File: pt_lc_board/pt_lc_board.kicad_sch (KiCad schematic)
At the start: 32 parts, among them J1 DSUB1, J2 DSUB2, J3 DSUB3, J4 PCIE Socket, U1 HX711_Breakout, U10 PCF8575_Breakout, U2 HX711_Breakout, U3 HX711_Breakout, U4 HX711_Breakout, U5 HX711_Breakout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

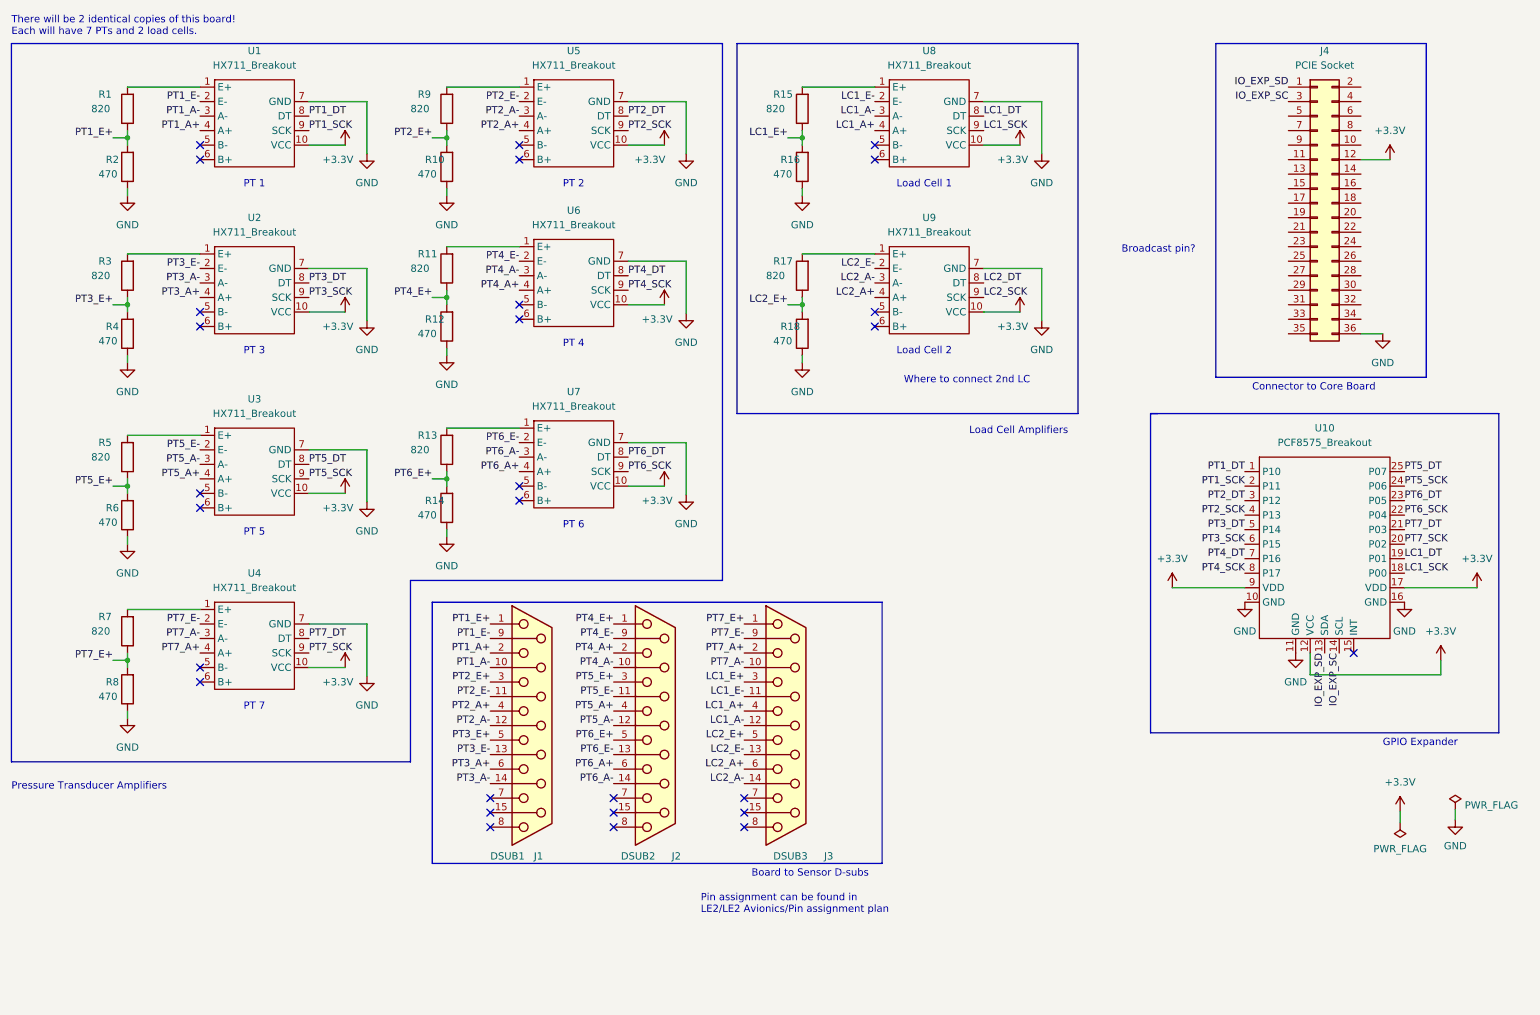
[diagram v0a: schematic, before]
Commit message: Almost done with layout. Need board-to-board connection.
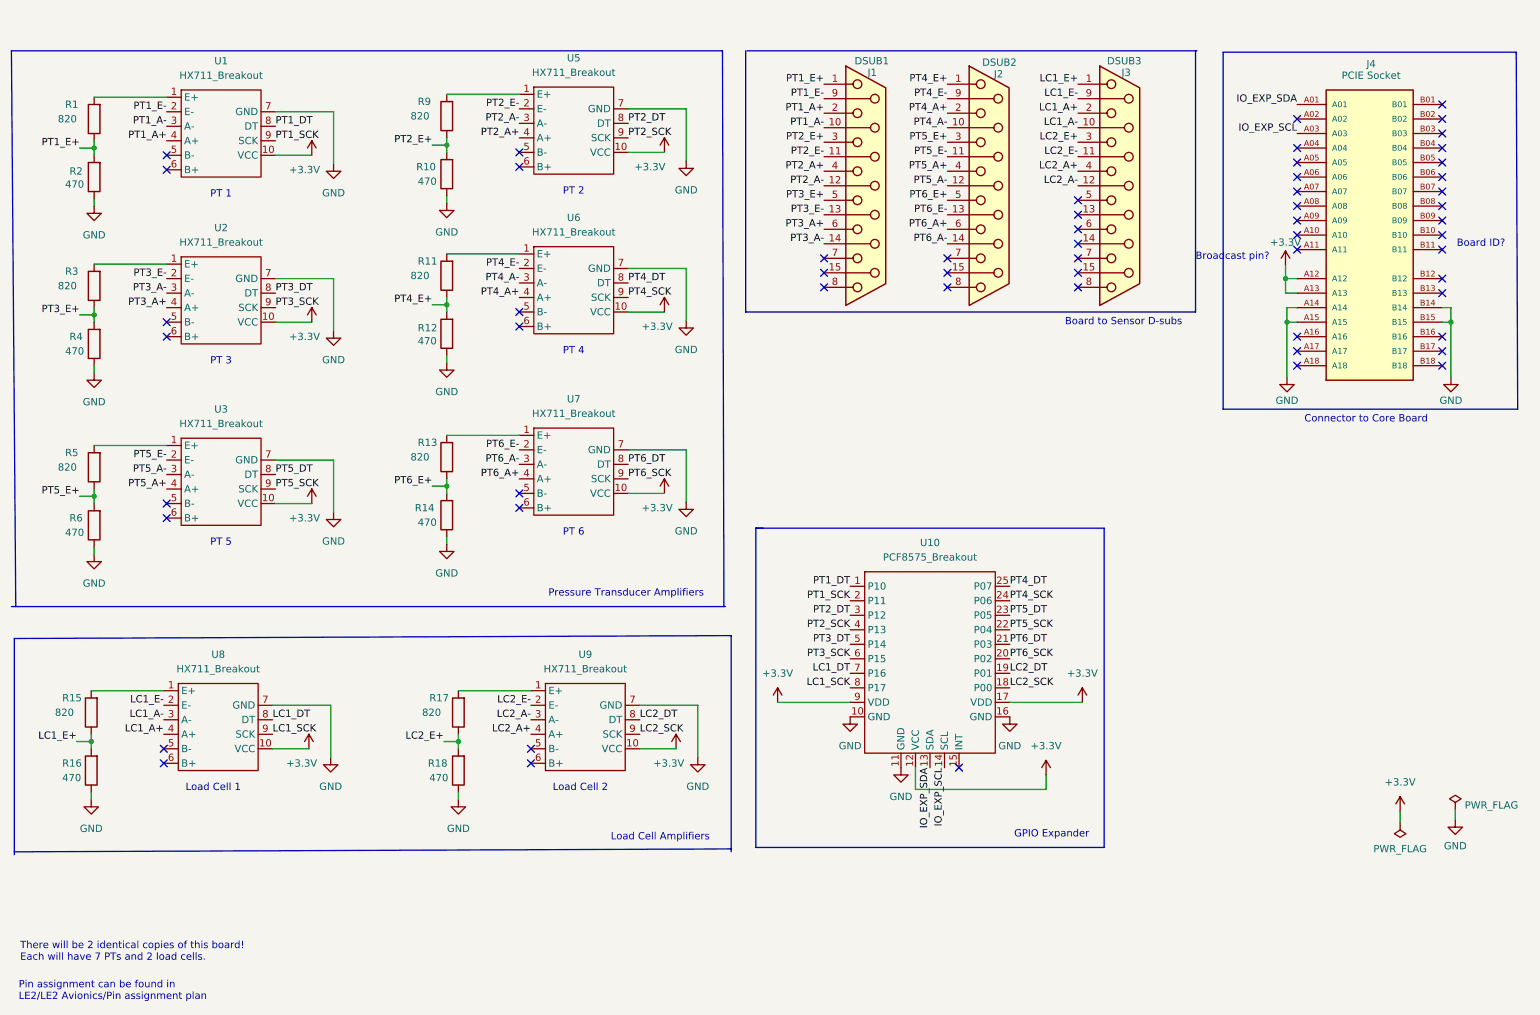
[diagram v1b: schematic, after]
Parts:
- removed R7: 820, Resistor_SMD:R_1206_3216Metric, symbol Device:R
- removed R8: 470, Resistor_SMD:R_1206_3216Metric, symbol Device:R
- removed U4: HX711_Breakout, symbol ELLIE_Symbol_Library:HX711_Breakout
- J1, J2, J3: footprint (none) -> Connector_Dsub:DSUB-15_Female_Horizontal_P2.77x2.84mm_EdgePinOffset7.70mm_Housed_MountingHolesOffset9.12mm
- J4: footprint (none) -> PCIE-LP-01-01-F-DV-A-TR:SAMTEC_PCIE-LP-01-01-F-DV-A-TR; symbol Connector_Generic:Conn_02x18_Odd_Even -> PCIE:PCIE-LP-01-01-F-DV-A-TR; MANUFACTURER (none) -> Samtec; MAXIMUM_PACKAGE_HEIGHT (none) -> 8.13mm; PARTREV (none) -> B; STANDARD (none) -> Manufacturer Recommendations
- U1, U2, U3, U5, U6, U7, U8, U9: footprint (none) -> Ellie_Project_Footprints:HX711_Breakout_Board
- U10: footprint (none) -> PCF8575_Breakout:PCF8575_Breakout
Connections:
- net PT7_A+ is gone; now on net LC1_A+: J3.2
- net PT7_A- is gone; now on net LC1_A-: J3.10 (P10)
- net PT7_DT is gone; now on net PT6_DT: U10.21 (P03)
- net PT7_E+ is gone; now on net LC1_E+: J3.1
- net PT7_E- is gone; now on net LC1_E-: J3.9 (P9)
- net PT7_SCK is gone; now on net PT6_SCK: U10.20 (P02)
- net +3V3: now also J4.A12, J4.A13; no longer J4.12 (Pin_12)
- net GND: now also J4.A14, J4.A15, J4.B14, J4.B15; no longer J4.36 (Pin_36)
- net LC1_A+: no longer J3.4
- net LC1_A-: no longer J3.12 (P12)
- net LC1_DT: now also U10.7 (P16); no longer U10.19 (P01)
- net LC1_E+: no longer J3.3
- net LC1_E-: no longer J3.11 (P111)
- net LC1_SCK: now also U10.8 (P17); no longer U10.18 (P00)
- net LC2_A+: now also J3.4; no longer J3.6
- net LC2_A-: now also J3.12 (P12); no longer J3.14 (P14)
- net LC2_DT: now also U10.19 (P01)
- net LC2_E+: now also J3.3; no longer J3.5
- net LC2_E-: now also J3.11 (P111); no longer J3.13 (P13)
- net LC2_SCK: now also U10.18 (P00)
- net PT4_DT: now also U10.25 (P07); no longer U10.7 (P16)
- net PT4_SCK: now also U10.24 (P06); no longer U10.8 (P17)
- net PT5_DT: now also U10.23 (P05); no longer U10.25 (P07)
- net PT5_SCK: now also U10.22 (P04); no longer U10.24 (P06)
- net PT6_DT: no longer U10.23 (P05)
- net PT6_SCK: no longer U10.22 (P04)
- net IO_EXP_SC renamed IO_EXP_SCL
- net IO_EXP_SCL: now also J4.A03; no longer J4.3 (Pin_3)
- net IO_EXP_SD renamed IO_EXP_SDA
- net IO_EXP_SDA: now also J4.A01; no longer J4.1 (Pin_1)
- no-connect marks 28 -> 58
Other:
- note added: "Board ID?"
- note removed: "PT 7"
- note removed: "Where to connect 2nd LC"
- moved on the sheet: J1, J2, J3, J4, R1, R10, R11, R12, R13, R14, R15, R16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

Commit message: Mostly finished with board.
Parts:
- added R10, R11, R9: 4.7k, Resistor_SMD:R_0603_1608Metric, symbol Device:R
- J4: value PCIE Socket -> PCIE Card Edge; footprint PCIE-LP-01-01-F-DV-A-TR:SAMTEC_PCIE-LP-01-01-F-DV-A-TR -> Connector_PCBEdge:BUS_PCIexpress_x1; symbol PCIE:PCIE-LP-01-01-F-DV-A-TR -> PCIE:PCIE-LP-01-01-F-DV-A-TR_(card_edge)
- R1, R13, R17: footprint Resistor_SMD:R_1206_3216Metric -> Resistor_SMD:R_0603_1608Metric
- R12: renamed from R5; footprint Resistor_SMD:R_1206_3216Metric -> Resistor_SMD:R_0603_1608Metric
- R14: renamed from R6; footprint Resistor_SMD:R_1206_3216Metric -> Resistor_SMD:R_0603_1608Metric
- R15: renamed from R14; footprint Resistor_SMD:R_1206_3216Metric -> Resistor_SMD:R_0603_1608Metric
- R16: renamed from R15; footprint Resistor_SMD:R_1206_3216Metric -> Resistor_SMD:R_0603_1608Metric
- R18: renamed from R16; footprint Resistor_SMD:R_1206_3216Metric -> Resistor_SMD:R_0603_1608Metric
- R19: renamed from R18; footprint Resistor_SMD:R_1206_3216Metric -> Resistor_SMD:R_0603_1608Metric
- R2: renamed from R9; footprint Resistor_SMD:R_1206_3216Metric -> Resistor_SMD:R_0603_1608Metric
- R3: renamed from R2; footprint Resistor_SMD:R_1206_3216Metric -> Resistor_SMD:R_0603_1608Metric
- R4: renamed from R10; footprint Resistor_SMD:R_1206_3216Metric -> Resistor_SMD:R_0603_1608Metric
- R5: renamed from R3; footprint Resistor_SMD:R_1206_3216Metric -> Resistor_SMD:R_0603_1608Metric
- R6: renamed from R11; footprint Resistor_SMD:R_1206_3216Metric -> Resistor_SMD:R_0603_1608Metric
- R7: renamed from R4; footprint Resistor_SMD:R_1206_3216Metric -> Resistor_SMD:R_0603_1608Metric
- R8: renamed from R12; footprint Resistor_SMD:R_1206_3216Metric -> Resistor_SMD:R_0603_1608Metric
- renumbered U5 to U2, U2 to U3, U6 to U4, U3 to U5, U7 to U6, U10 to U7
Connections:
- net GND: now also R10.1, R11.1
- net IO_EXP_SCL: now also J4.A3; no longer J4.A03
- net IO_EXP_SDA: now also J4.A1; no longer J4.A01
- net Board_ID: now reaches J4.B11
- net Board_ID: now also R10.2, R11.2, R9.1
- net +5V: now reaches J4.B12
- net +5V: now also J4.B13, R9.2
- no-connect marks 58 -> 55
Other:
- note added: "Board ID"
- note added: "PT board 1: board_ID = 2.5, connects 1 resistor. PT board 2: board_ID = 3.0, connects 2 resistors."
- note removed: "Board ID?"
- note removed: "Broadcast pin?"
- moved on the sheet: R13, R15, R2, R4, R6, R8, U2, U4, U6

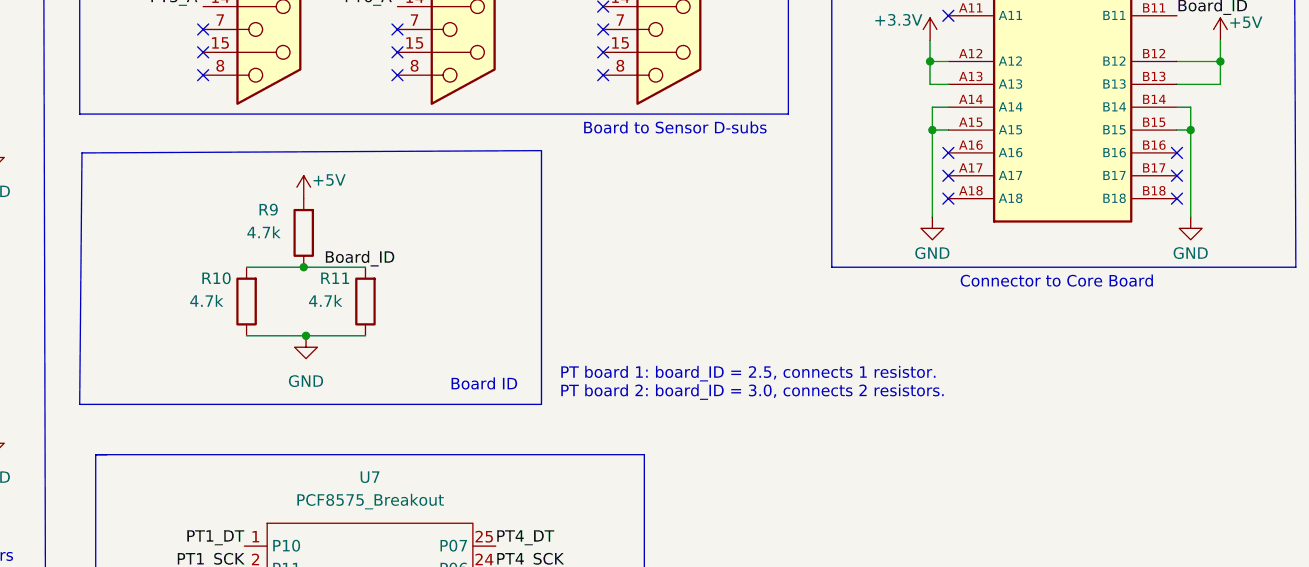
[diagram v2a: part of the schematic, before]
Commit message: Updated board_ID.
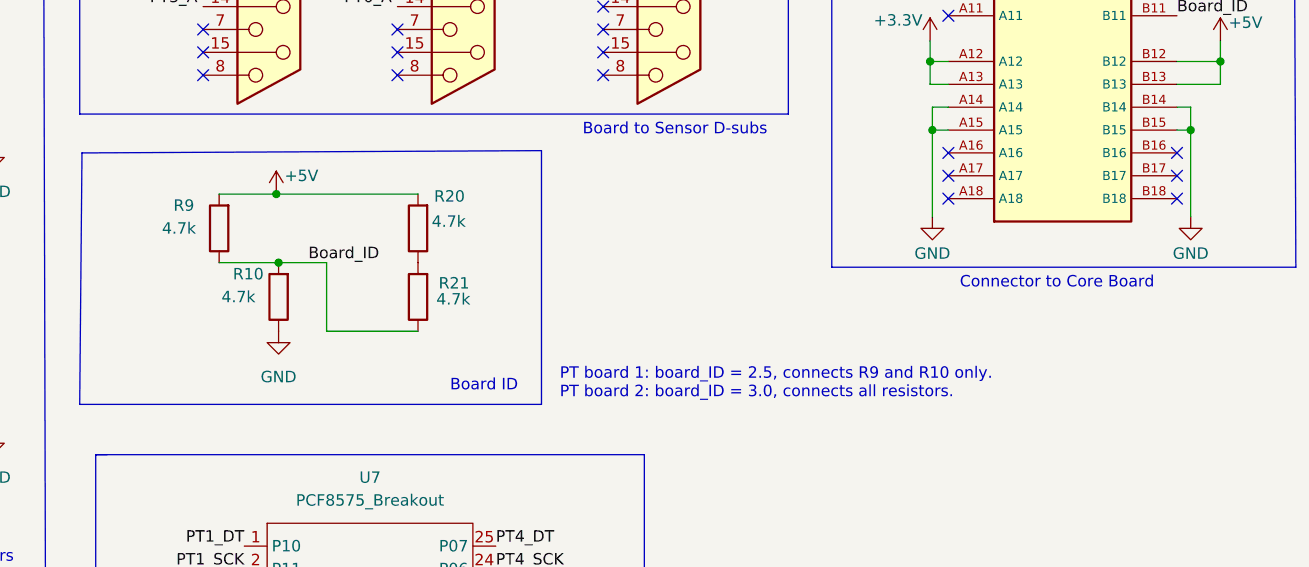
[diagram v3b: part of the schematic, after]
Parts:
- added R21: 4.7k, Resistor_SMD:R_0603_1608Metric, symbol Device:R
- renumbered R9 to R10, R11 to R20, R10 to R9
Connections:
- net +5V: now also R20.2, R9.2; no longer R10.2
- net Board_ID: now also R10.2, R9.1, R21.1; no longer R10.1, R20.2, R9.2
- net GND: now also R10.1; no longer R20.1, R9.1
- new net: R20.1, R21.2
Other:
- note added: "PT board 1: board_ID = 2.5, connects R9 and R10 only. PT board 2: board_ID = 3.0, connects all resistors."
- note removed: "PT board 1: board_ID = 2.5, connects 1 resistor. PT board 2: board_ID = 3.0, connects 2 resistors."
- moved on the sheet: R10, R20, R9
